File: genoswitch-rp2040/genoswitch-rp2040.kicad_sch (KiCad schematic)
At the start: 30 parts, among them J1 USB_B_Micro, SW1 BOOTSEL, U1 NCP1117-3.3_SOT223, U2 W25Q128JVS, U3 RP2040, U4 MCP1501-10xCH, Y1 ABLS-12.000MHZ-B4-T

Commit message: Add a Serial Wire Debug header
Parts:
- added J2: Conn_01x03_Socket-PicoDebug, Connector_PinHeader_2.54mm:PinHeader_1x03_P2.54mm_Vertical, symbol Connector:Conn_01x03_Socket
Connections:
- net GND: now also J2.2 (Pin_2)
- net SWCLK: now reaches U3.24 (SWCLK)
- net SWCLK: now also J2.1 (Pin_1)
- net SWDIO: now reaches U3.25 (SWD)
- net SWDIO: now also J2.3 (Pin_3)
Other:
- note added: "Serial Wire Debug Header (2.54mm pitch)"
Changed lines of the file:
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@@
+    (stroke (width 0) (type default))
+  )
+  (wire (pts (xy 322.58 142.24) (xy 331.47 142.24))
     (stroke (width 0) (type default))
   )
@@
     (stroke (width 0) (type default))
   )
+  (wire (pts (xy 49.53 132.08) (xy 55.88 132.08))
+    (stroke (width 0) (type default))
+  )
   (wire (pts (xy 170.18 40.64) (xy 160.02 40.64))
     (stroke (width 0) (type default))
@@
     (stroke (width 0) (type default))
   )
+  (wire (pts (xy 322.58 137.16) (xy 331.47 137.16))
+    (stroke (width 0) (type default))
+  )
   (wire (pts (xy 49.53 111.76) (xy 55.88 111.76))
     (stroke (width 0) (type default))
@@
     (stroke (width 0) (type default))
   )
+  (wire (pts (xy 330.2 143.51) (xy 330.2 139.7))
+    (stroke (width 0) (type default))
+  )
   (wire (pts (xy 170.18 30.48) (xy 170.18 31.75))
     (stroke (width 0) (type default))
@@
     (stroke (width 0) (type default))
   )
+  (wire (pts (xy 49.53 134.62) (xy 55.88 134.62))
+    (stroke (width 0) (type default))
+  )
   (wire (pts (xy 397.51 223.52) (xy 397.51 222.25))
     (stroke (width 0) (type default))
@@
     (stroke (width 0) (type default))
   )
+  (wire (pts (xy 330.2 139.7) (xy 331.47 139.7))
+    (stroke (width 0) (type default))
+  )
   (wire (pts (xy 85.09 45.72) (xy 87.63 45.72))
     (stroke (width 0) (type default))
@@
   (wire (pts (xy 361.95 36.83) (xy 361.95 48.26))
     (stroke (width 0) (type default))
+  )
+  (rectangle (start 320.04 127) (end 405.13 151.13)
+    (stroke (width 0) (type default))
+    (fill (type none))
   )
   (rectangle (start 158.75 13.97) (end 236.22 57.15)
@@
     (effects (font (size 2.54 2.54)) (justify left bottom))
   )
+  (text "Serial Wire Debug Header (2.54mm pitch)" (at 322.58 133.35 0)
+    (effects (font (size 2.54 2.54)) (justify left bottom))
+  )
   (text "Crystal" (at 331.47 158.75 0)
     (effects (font (size 2.54 2.54)) (justify left bottom))
@@
     (effects (font (size 1.27 1.27)) (justify left bottom))
   )
+  (label "SWDIO" (at 49.53 134.62 0) (fields_autoplaced)
+    (effects (font (size 1.27 1.27)) (justify left bottom))
+  )
   (label "XOUT" (at 49.53 121.92 0) (fields_autoplaced)
     (effects (font (size 1.27 1.27)) (justify left bottom))
@@
     (effects (font (size 1.27 1.27)) (justify left bottom))
   )
+  (label "SWCLK" (at 49.53 132.08 0) (fields_autoplaced)
+    (effects (font (size 1.27 1.27)) (justify left bottom))
+  )
+  (label "SWCLK" (at 322.58 137.16 0) (fields_autoplaced)
+    (effects (font (size 1.27 1.27)) (justify left bottom))
+  )
   (label "QSPI_SD3" (at 372.11 48.26 90) (fields_autoplaced)
     (effects (font (size 1.27 1.27)) (justify left bottom))
@@
   (label "MCP1501_SHDN" (at 121.92 121.92 180) (fields_autoplaced)
     (effects (font (size 1.27 1.27)) (justify right bottom))
+  )
+  (label "SWDIO" (at 322.58 142.24 0) (fields_autoplaced)
+    (effects (font (size 1.27 1.27)) (justify left bottom))
   )
   (label "QSPI_SCLK" (at 361.95 48.26 90) (fields_autoplaced)
@@
     )
   )
+  (symbol (lib_id "Connector:Conn_01x03_Socket") (at 336.55 139.7 0) (unit 1)
+    (in_bom yes) (on_board yes) (dnp no)
+    (property "Reference" "J2" (at 337.82 138.43 0)
+      (effects (font (size 1.27 1.27)) (justify left))
+    )
+    (property "Value" "Conn_01x03_Socket-PicoDebug" (at 337.82 140.97 0)
+      (effects (font (size 1.27 1.27)) (justify left))
+    )
+    (property "Footprint" "Connector_PinHeader_2.54mm:PinHeader_1x03_P2.54mm_Vertical" (at 336.55 139.7 0)
+      (effects (font (size 1.27 1.27)) hide)
+    )
+    (property "Datasheet" "~" (at 336.55 139.7 0)
+      (effects (font (size 1.27 1.27)) hide)
+    )
+    (pin "1")
+    (pin "2")
+    (pin "3")
+    (instances
+      (project "genoswitch-rp2040"
+        (path "/2e7ee4d9-1204-4a0f-bb2c-fb0f0d4af2cf"
+          (reference "J2") (unit 1)
+        )
+      )
+    )
+  )
   (symbol (lib_id "Device:C") (at 50.8 40.64 0) (unit 1)
     (in_bom yes) (on_board yes) (dnp no) (fields_autoplaced)
@@
         )
       )
+    )
+  )
+  (symbol (lib_id "power:GND") (at 330.2 143.51 0) (unit 1)
+    (in_bom yes) (on_board yes) (dnp no) (fields_autoplaced)
+    (property "Reference" "#PWR023" (at 330.2 149.86 0)
+      (effects (font (size 1.27 1.27)) hide)
+    )
+    (property "Value" "GND" (at 330.2 148.59 0)
+      (effects (font (size 1.27 1.27)))
+    )
+    (property "Footprint" "" (at 330.2 143.51 0)
+      (effects (font (size 1.27 1.27)) hide)
+    )
+    (property "Datasheet" "" (at 330.2 143.51 0)
+      (effects (font (size 1.27 1.27)) hide)
+    )
+    (pin "1")
+    (instances
+      (project "genoswitch-rp2040"
+        (path "/2e7ee4d9-1204-4a0f-bb2c-fb0f0d4af2cf"
+          (reference "#PWR023") (unit 1)
+        )
+      )

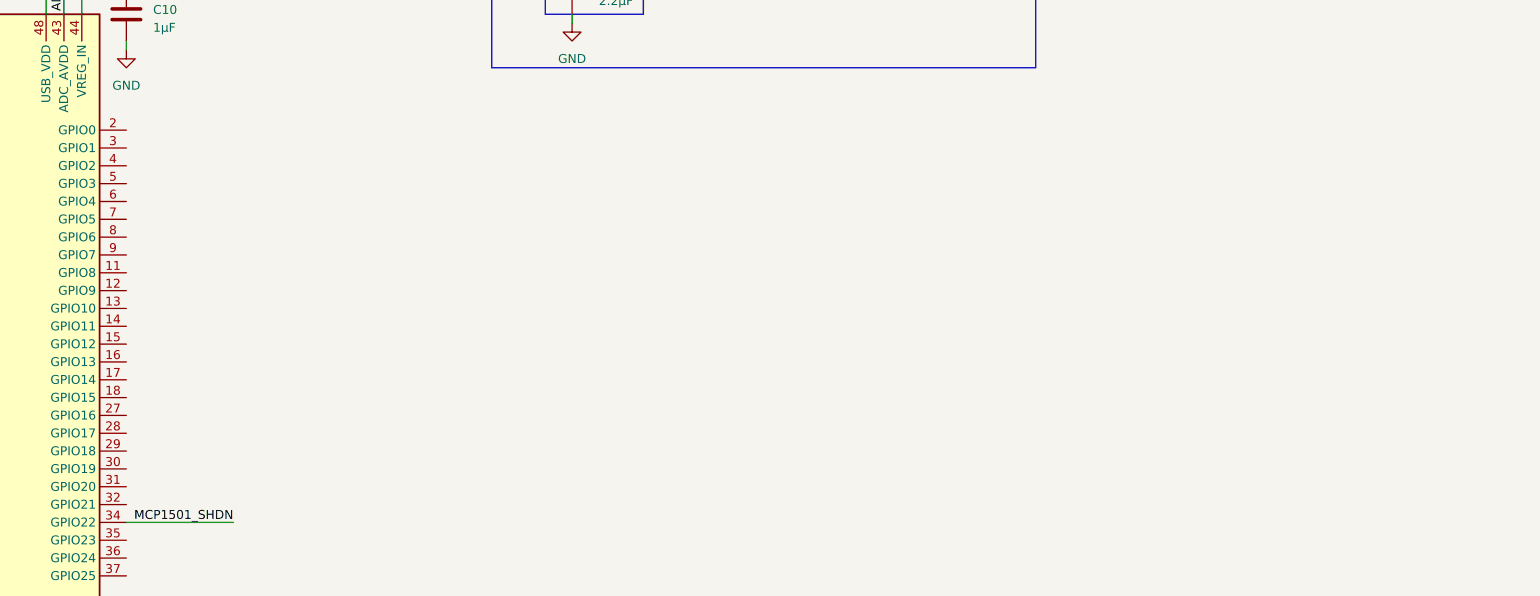
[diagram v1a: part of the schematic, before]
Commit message: Add HW SPI MCP3008s
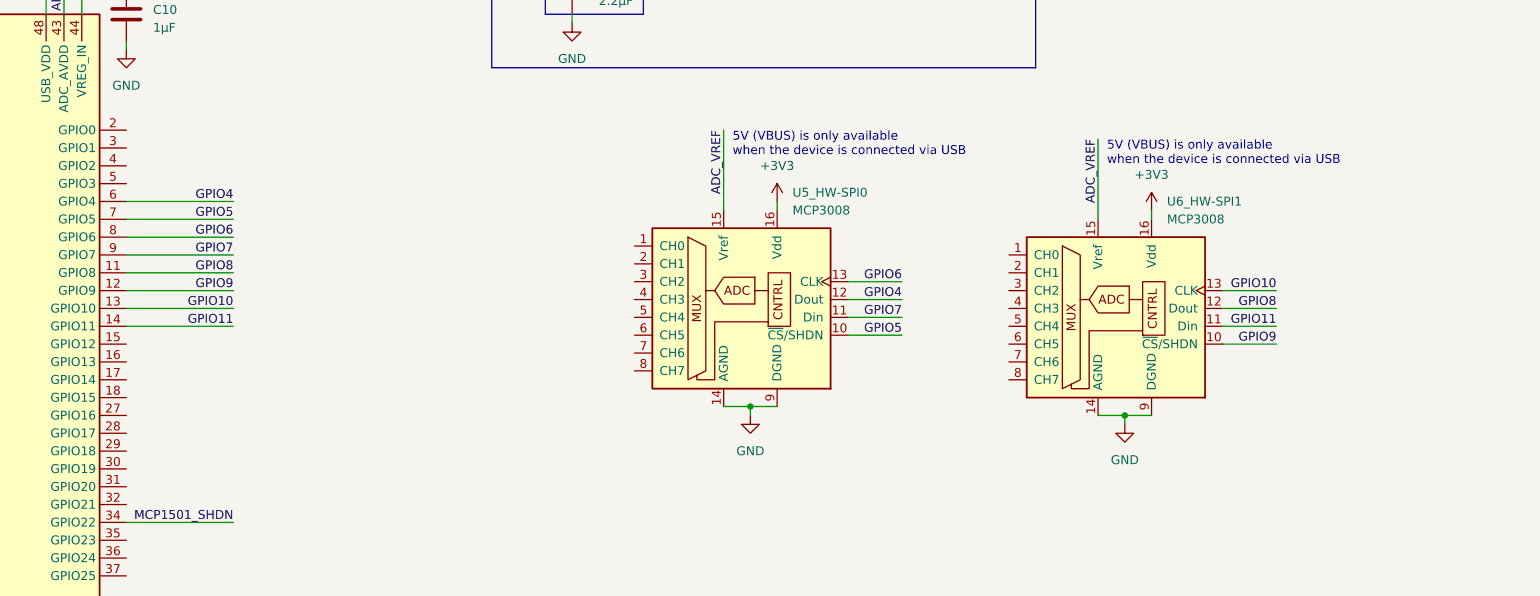
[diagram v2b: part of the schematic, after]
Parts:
- added U5_HW-SPI0, U6_HW-SPI1: MCP3008, Package_SO:SOIC-16_3.9x9.9mm_P1.27mm, symbol Analog_ADC:MCP3008
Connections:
- net +3V3: now also U5_HW-SPI0.16 (Vdd), U6_HW-SPI1.16 (Vdd)
- net ADC_VREF: now also U5_HW-SPI0.15 (Vref), U6_HW-SPI1.15 (Vref)
- net GND: now also U5_HW-SPI0.14 (AGND), U5_HW-SPI0.9 (DGND), U6_HW-SPI1.14 (AGND), U6_HW-SPI1.9 (DGND)
- net GPIO8: now reaches U3.11 (GPIO8)
- net GPIO8: now also U6_HW-SPI1.12 (Dout)
- net GPIO9: now reaches U3.12 (GPIO9)
- net GPIO9: now also U6_HW-SPI1.10 (~{CS}/SHDN)
- net GPIO10: now reaches U3.13 (GPIO10)
- net GPIO10: now also U6_HW-SPI1.13 (CLK)
- net GPIO11: now reaches U3.14 (GPIO11)
- net GPIO11: now also U6_HW-SPI1.11 (Din)
- net GPIO4: now reaches U3.6 (GPIO4)
- net GPIO4: now also U5_HW-SPI0.12 (Dout)
- net GPIO5: now reaches U3.7 (GPIO5)
- net GPIO5: now also U5_HW-SPI0.10 (~{CS}/SHDN)
- net GPIO6: now reaches U3.8 (GPIO6)
- net GPIO6: now also U5_HW-SPI0.13 (CLK)
- net GPIO7: now reaches U3.9 (GPIO7)
- net GPIO7: now also U5_HW-SPI0.11 (Din)
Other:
- note added: "5V (VBUS) is only available when the device is connected via USB"

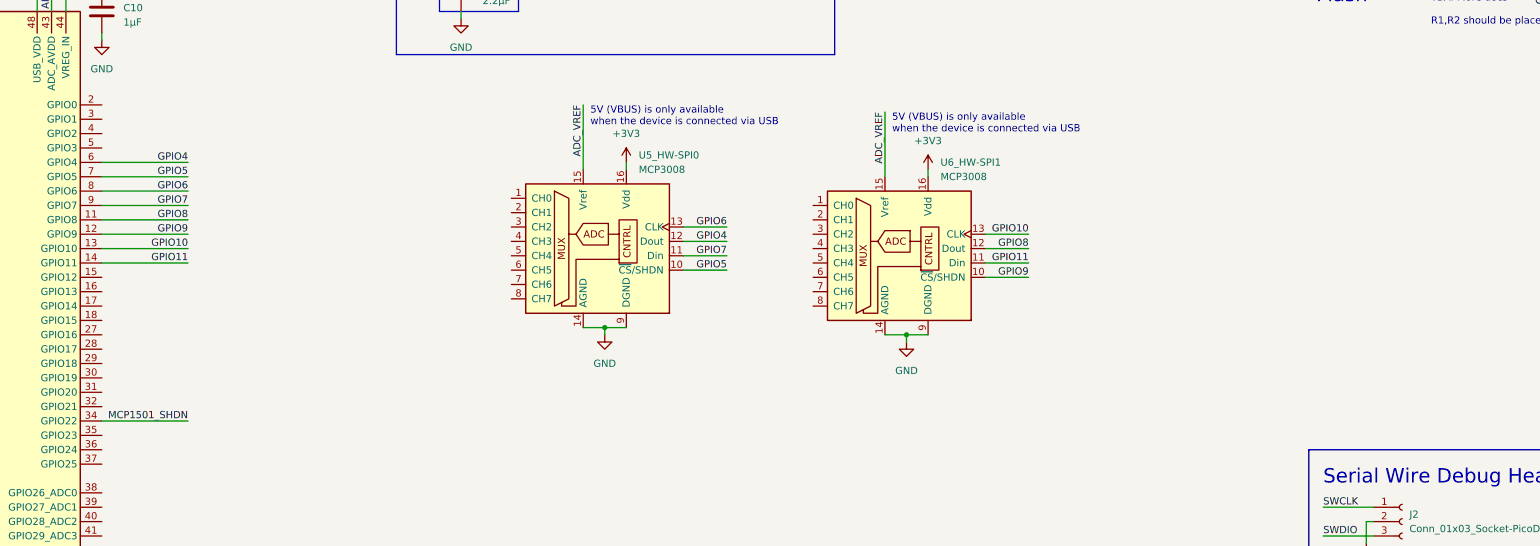
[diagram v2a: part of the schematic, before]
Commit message: Add PIO SPI MCP3008s
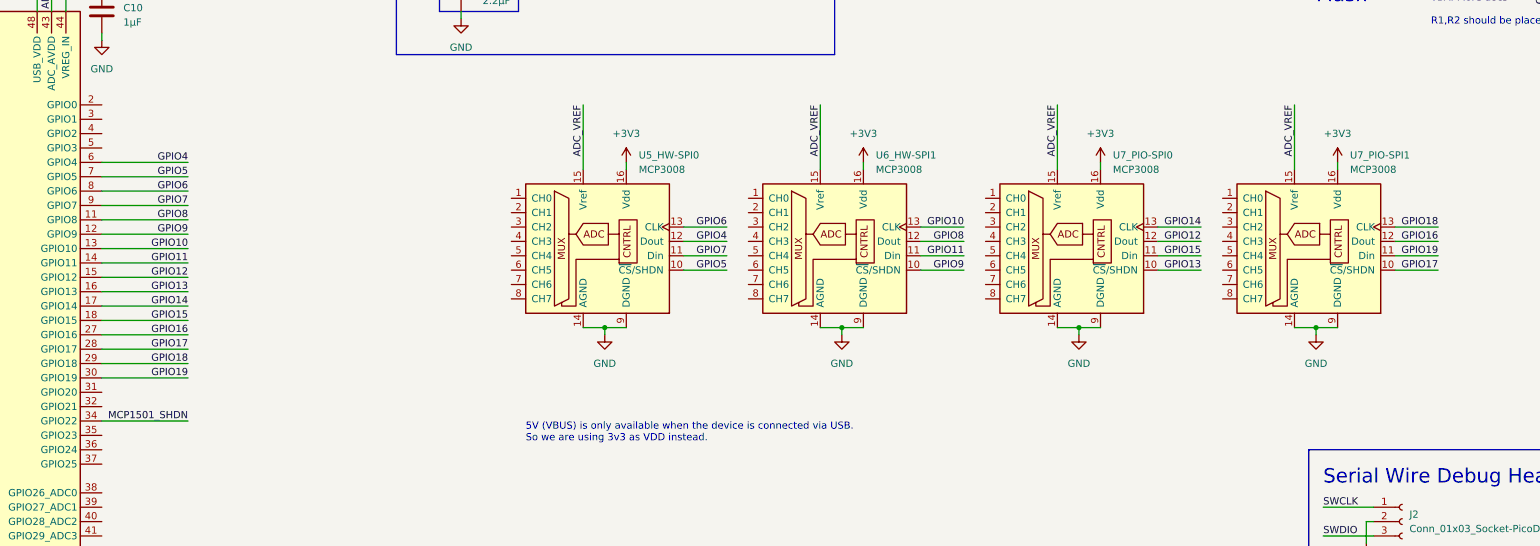
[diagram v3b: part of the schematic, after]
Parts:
- added U7_PIO-SPI0, U7_PIO-SPI1: MCP3008, Package_SO:SOIC-16_3.9x9.9mm_P1.27mm, symbol Analog_ADC:MCP3008
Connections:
- net +3V3: now also U7_PIO-SPI0.16 (Vdd), U7_PIO-SPI1.16 (Vdd)
- net ADC_VREF: now also U7_PIO-SPI0.15 (Vref), U7_PIO-SPI1.15 (Vref)
- net GND: now also U7_PIO-SPI0.14 (AGND), U7_PIO-SPI0.9 (DGND), U7_PIO-SPI1.14 (AGND), U7_PIO-SPI1.9 (DGND)
- net GPIO12: now reaches U3.15 (GPIO12)
- net GPIO12: now also U7_PIO-SPI0.12 (Dout)
- net GPIO13: now reaches U3.16 (GPIO13)
- net GPIO13: now also U7_PIO-SPI0.10 (~{CS}/SHDN)
- net GPIO14: now reaches U3.17 (GPIO14)
- net GPIO14: now also U7_PIO-SPI0.13 (CLK)
- net GPIO15: now reaches U3.18 (GPIO15)
- net GPIO15: now also U7_PIO-SPI0.11 (Din)
- net GPIO16: now reaches U3.27 (GPIO16)
- net GPIO16: now also U7_PIO-SPI1.12 (Dout)
- net GPIO17: now reaches U3.28 (GPIO17)
- net GPIO17: now also U7_PIO-SPI1.10 (~{CS}/SHDN)
- net GPIO18: now reaches U3.29 (GPIO18)
- net GPIO18: now also U7_PIO-SPI1.13 (CLK)
- net GPIO19: now reaches U3.30 (GPIO19)
- net GPIO19: now also U7_PIO-SPI1.11 (Din)
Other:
- note added: "5V (VBUS) is only available when the device is connected via USB. So we are using 3v3 as VDD instead."
- note removed: "5V (VBUS) is only available when the device is connected via USB"
- moved on the sheet: U6_HW-SPI1

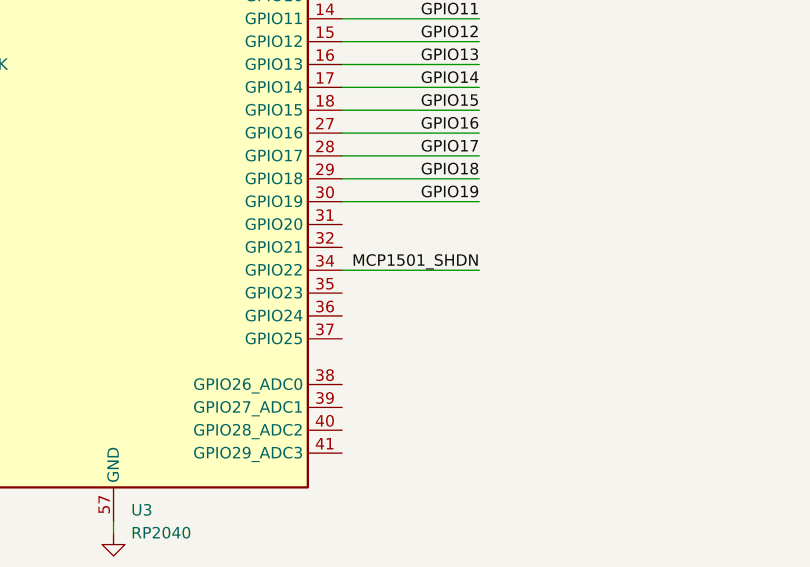
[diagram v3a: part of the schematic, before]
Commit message: Change MCP1501_SHDN to GP24
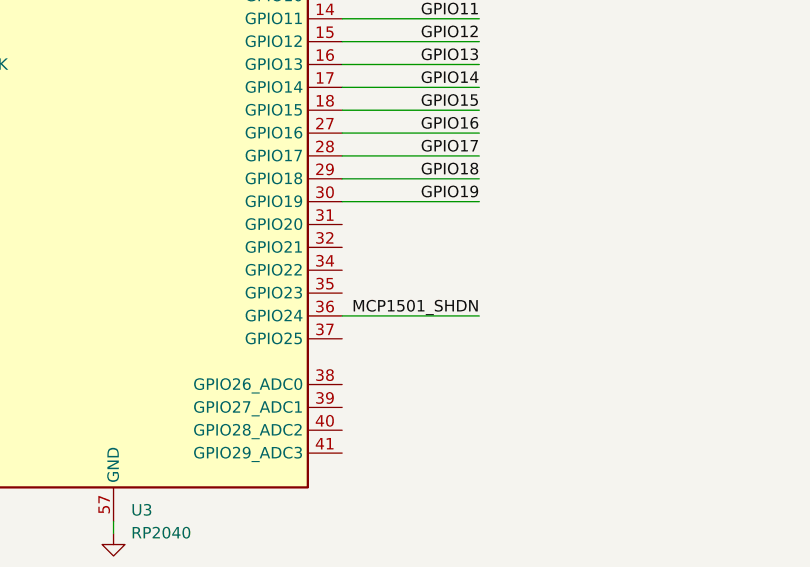
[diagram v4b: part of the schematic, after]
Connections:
- net MCP1501_SHDN: now also U3.36 (GPIO24); no longer U3.34 (GPIO22)
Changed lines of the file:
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@@
-    (stroke (width 0) (type default))
-  )
-  (wire (pts (xy 106.68 121.92) (xy 121.92 121.92))
     (stroke (width 0) (type default))
   )
@@
   )
   (wire (pts (xy 120.65 33.02) (xy 107.95 33.02))
+    (stroke (width 0) (type default))
+  )
+  (wire (pts (xy 106.68 127) (xy 121.92 127))
     (stroke (width 0) (type default))
   )
@@
     (effects (font (size 1.27 1.27)) (justify right bottom))
   )
+  (label "MCP1501_SHDN" (at 121.92 127 180) (fields_autoplaced)
+    (effects (font (size 1.27 1.27)) (justify right bottom))
+  )
   (label "GPIO5" (at 217.17 95.25 180) (fields_autoplaced)
     (effects (font (size 1.27 1.27)) (justify right bottom))
@@
     (effects (font (size 1.27 1.27)) (justify right bottom))
   )
-  (label "MCP1501_SHDN" (at 121.92 121.92 180) (fields_autoplaced)
-    (effects (font (size 1.27 1.27)) (justify right bottom))
-  )
